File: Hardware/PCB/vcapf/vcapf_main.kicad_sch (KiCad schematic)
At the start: 42 parts, among them Q1 2N3906, Q2 2N3906, U1 LM13700, U2 TL074, U3 TL072

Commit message: Match transistors
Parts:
- Q1, Q2: value 2N3906 -> (none)
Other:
- moved on the sheet: C10, C4, C5, C7, C8, C9, U1B, U1D, U1E, U2E, U3C

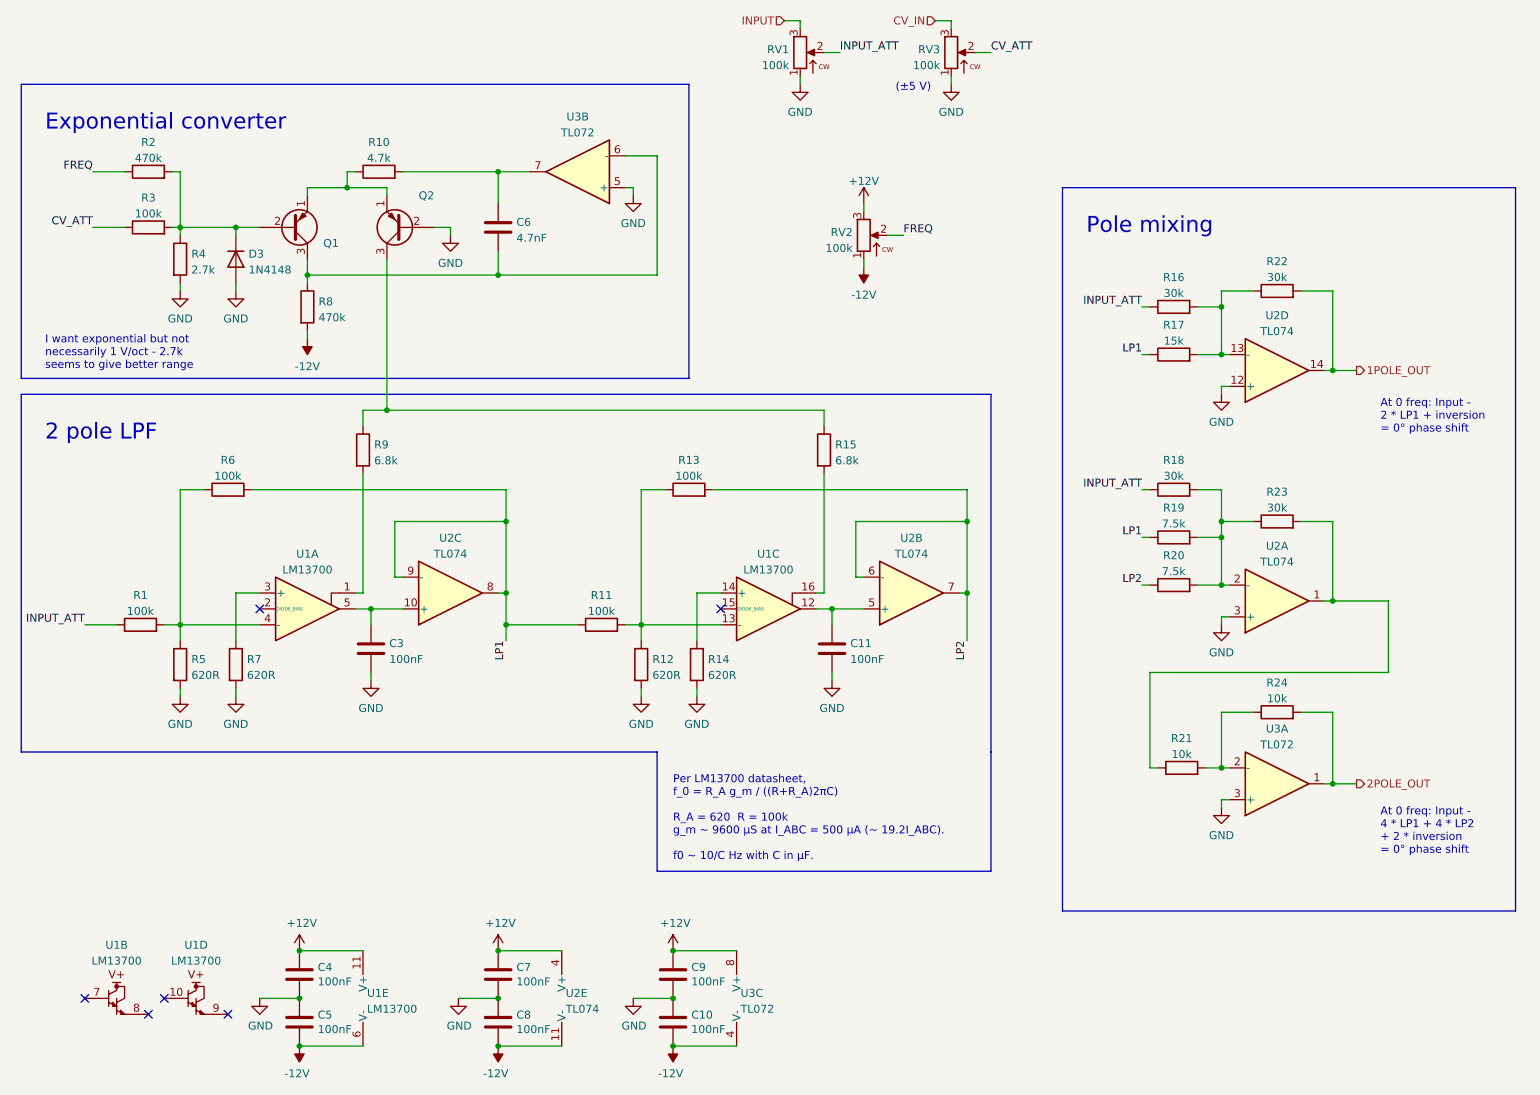
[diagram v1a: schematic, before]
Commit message: Pre fab tweaks, unreverse jacks, Gerbers
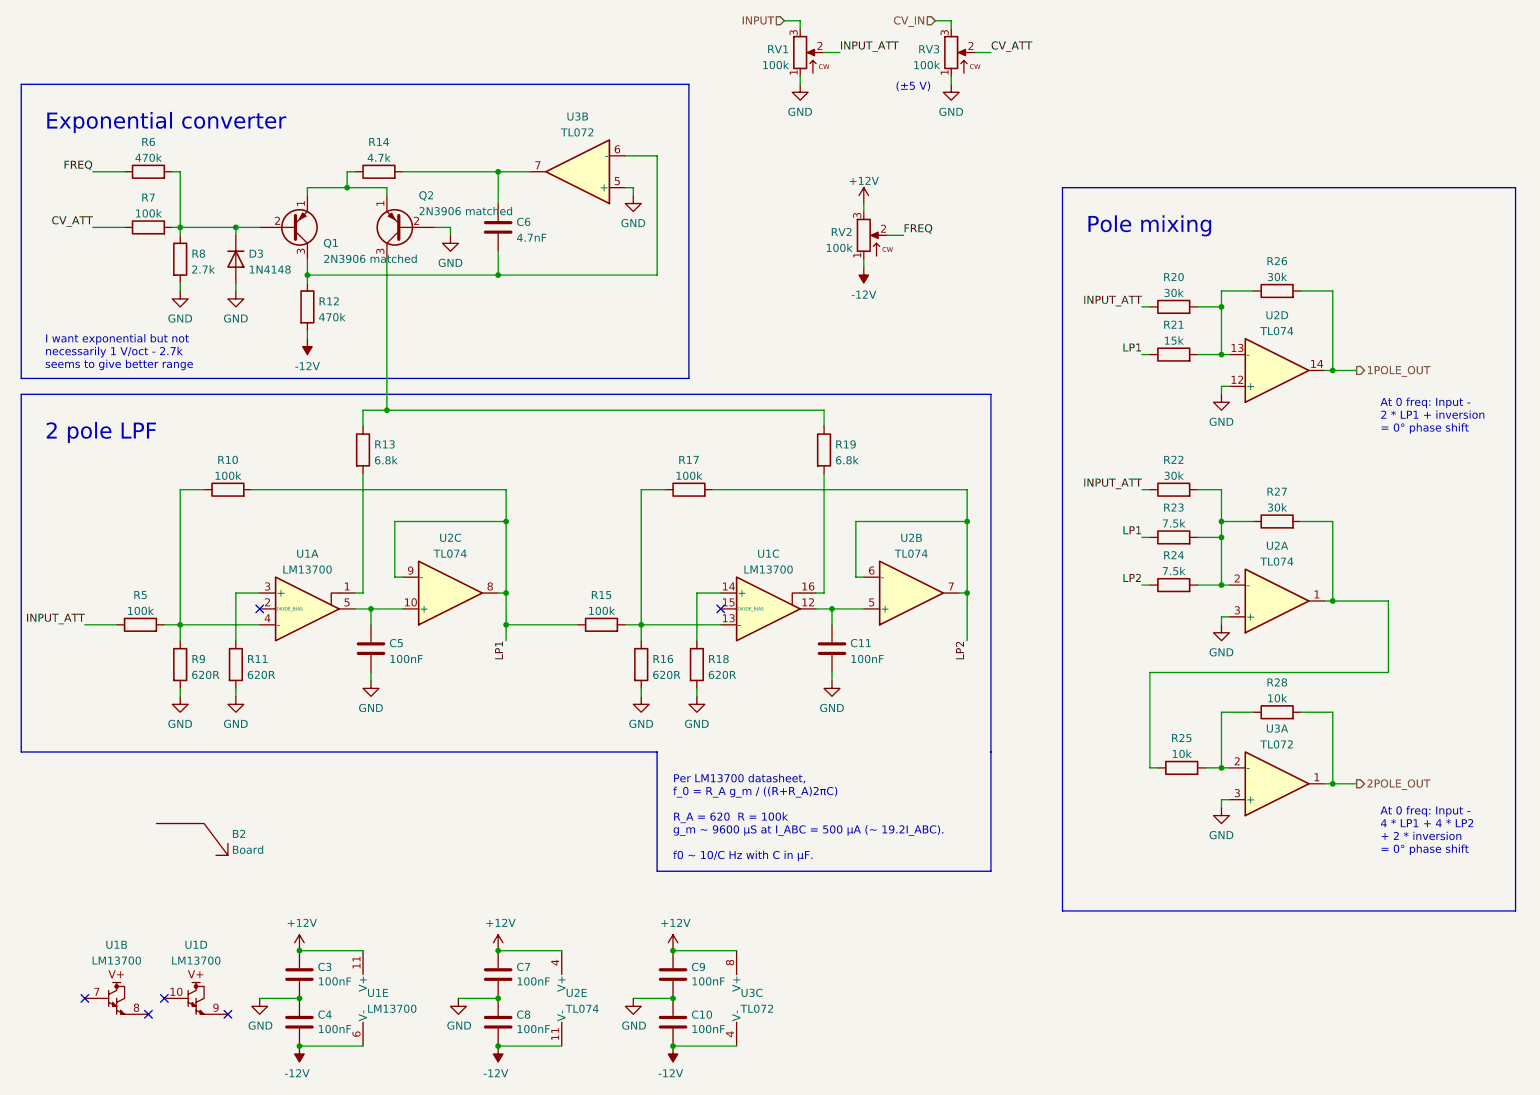
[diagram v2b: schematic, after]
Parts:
- added B2: Board, ao_tht:Board_Marker, symbol ao_symbols:Board
- Q1, Q2: value (none) -> 2N3906 matched
- renumbered C4 to C3, C5 to C4, C3 to C5, R6 to R10, R7 to R11, R8 to R12, R9 to R13, R10 to R14, R11 to R15, R12 to R16, R13 to R17, R14 to R18, R15 to R19, R16 to R20, R17 to R21, R18 to R22, R19 to R23, R20 to R24, R21 to R25, R22 to R26, R23 to R27, R24 to R28, R1 to R5, R2 to R6, R3 to R7, R4 to R8, R5 to R9

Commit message: Post fab updates
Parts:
- C11, C5: SKU (none) -> A-564
- RV1, RV2, RV3: SKU (none) -> A-1628
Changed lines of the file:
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@@
+      (effects (font (size 1.27 1.27)) hide)
+    )
+    (property "Description" "1/4 watt resistor, metal film" (id 5) (at 57.15 125.73 0)
       (effects (font (size 1.27 1.27)) hide)
     )
@@
     )
     (property "SKU" "A-553" (id 5) (at 67.31 175.26 0)
+      (effects (font (size 1.27 1.27)) hide)
+    )
+    (property "Description" "Ceramic capacitor, 2.5 mm pitch" (id 6) (at 67.31 175.26 0)
       (effects (font (size 1.27 1.27)) hide)
     )
@@
       (effects (font (size 1.27 1.27)) hide)
     )
+    (property "Description" "Ceramic capacitor, 2.5 mm pitch" (id 6) (at 127 182.88 0)
+      (effects (font (size 1.27 1.27)) hide)
+    )
     (pin "1")
     (pin "2")
@@
     )
     (property "Vendor" "Tayda" (id 4) (at 48.26 60.96 0)
+      (effects (font (size 1.27 1.27)) hide)
+    )
+    (property "Description" "1/4 watt resistor, metal film" (id 5) (at 48.26 60.96 0)
       (effects (font (size 1.27 1.27)) hide)
     )
@@
       (effects (font (size 1.27 1.27)) hide)
     )
+    (property "Description" "1/4 watt resistor, metal film" (id 5) (at 207.01 105.41 0)
+      (effects (font (size 1.27 1.27)) hide)
+    )
     (pin "1")
     (pin "2")
@@
     )
     (property "Vendor" "Tayda" (id 4) (at 130.81 125.73 0)
+      (effects (font (size 1.27 1.27)) hide)
+    )
+    (property "Description" "1/4 watt resistor, metal film" (id 5) (at 130.81 125.73 0)
       (effects (font (size 1.27 1.27)) hide)
     )
@@
       (effects (font (size 1.27 1.27)) hide)
     )
+    (property "Description" "Ceramic capacitor, 2.5 mm pitch" (id 6) (at 99.06 175.26 0)
+      (effects (font (size 1.27 1.27)) hide)
+    )
     (pin "1")
     (pin "2")
@@
     )
     (property "Vendor" "Tayda" (id 4) (at 68.58 68.58 0)
+      (effects (font (size 1.27 1.27)) hide)
+    )
+    (property "Description" "1/4 watt resistor, metal film" (id 5) (at 68.58 68.58 0)
       (effects (font (size 1.27 1.27)) hide)
     )
@@
       (effects (font (size 1.27 1.27)) hide)
     )
+    (property "Description" "1/4 watt resistor, metal film" (id 5) (at 207.01 68.58 0)
+      (effects (font (size 1.27 1.27)) hide)
+    )
     (pin "1")
     (pin "2")
@@
     )
     (property "Vendor" "Tayda" (id 4) (at 80.01 46.99 0)
+      (effects (font (size 1.27 1.27)) hide)
+    )
+    (property "Description" "1/4 watt resistor, metal film" (id 5) (at 80.01 46.99 0)
       (effects (font (size 1.27 1.27)) hide)
     )
@@
       (effects (font (size 1.27 1.27)) hide)
     )
+    (property "Description" "1/4 watt resistor, metal film" (id 5) (at 208.28 142.24 0)
+      (effects (font (size 1.27 1.27)) hide)
+    )
     (pin "1")
     (pin "2")
@@
     )
     (property "Vendor" "Tayda" (id 4) (at 77.47 91.44 0)
+      (effects (font (size 1.27 1.27)) hide)
+    )
+    (property "Description" "1/4 watt resistor, metal film" (id 5) (at 77.47 91.44 0)
       (effects (font (size 1.27 1.27)) hide)
     )
@@
       (effects (font (size 1.27 1.27)) hide)
     )
+    (property "Description" "1/4 watt resistor, metal film" (id 5) (at 121.92 125.73 0)
+      (effects (font (size 1.27 1.27)) hide)
+    )
     (pin "1")
     (pin "2")
@@
     )
     (property "Vendor" "Tayda" (id 4) (at 41.91 119.38 0)
+      (effects (font (size 1.27 1.27)) hide)
+    )
+    (property "Description" "1/4 watt resistor, metal film" (id 5) (at 41.91 119.38 0)
       (effects (font (size 1.27 1.27)) hide)
     )
@@
       (effects (font (size 1.27 1.27)) hide)
     )
+    (property "Description" "1/4 watt resistor, metal film" (id 5) (at 115.57 119.38 0)
+      (effects (font (size 1.27 1.27)) hide)
+    )
     (pin "1")
     (pin "2")
@@
       (effects (font (size 1.27 1.27)) hide)
     )
+    (property "Description" "Polyester capacitor" (id 5) (at 152.4 123.19 0)
+      (effects (font (size 1.27 1.27)) hide)
+    )
+    (property "SKU" "A-564" (id 6) (at 152.4 123.19 0)
+      (effects (font (size 1.27 1.27)) hide)
+    )
     (pin "1")
     (pin "2")
@@
       (effects (font (size 1.27 1.27)) hide)
     )
+    (property "Description" "1/4 watt resistor, metal film" (id 5) (at 43.18 55.88 0)
+      (effects (font (size 1.27 1.27)) hide)
+    )
     (pin "1")
     (pin "2")
@@
     )
     (property "Vendor" "Tayda" (id 4) (at 99.06 55.88 0)
+      (effects (font (size 1.27 1.27)) hide)
+    )
+    (property "Description" "Ceramic capacitor, 2.5 mm pitch" (id 5) (at 99.06 55.88 0)
       (effects (font (size 1.27 1.27)) hide)
     )
@@
       (effects (font (size 1.27 1.27)) hide)
     )
+    (property "Description" "Ceramic capacitor, 2.5 mm pitch" (id 6) (at 127 175.26 0)
+      (effects (font (size 1.27 1.27)) hide)
+    )
     (pin "1")
     (pin "2")
@@
     )
     (property "Vendor" "Tayda" (id 4) (at 151.13 91.44 0)
+      (effects (font (size 1.27 1.27)) hide)
+    )
+    (property "Description" "1/4 watt resistor, metal film" (id 5) (at 151.13 91.44 0)
       (effects (font (size 1.27 1.27)) hide)
     )
@@
     )
     (property "Vendor" "Tayda" (id 4) (at 171.45 27.94 0)
+      (effects (font (size 1.27 1.27)) hide)
+    )
+    (property "Description" "Linear potentiometer, 16 mm, PCB mount, vertical" (id 5) (at 171.45 27.94 0)
+      (effects (font (size 1.27 1.27)) hide)
+    )
+    (property "SKU" "A-1628" (id 6) (at 171.45 27.94 0)
       (effects (font (size 1.27 1.27)) hide)
     )
@@
     )
     (property "SKU" "A-553" (id 5) (at 99.06 182.88 0)
+      (effects (font (size 1.27 1.27)) hide)
+    )
+    (property "Description" "Ceramic capacitor, 2.5 mm pitch" (id 6) (at 99.06 182.88 0)
       (effects (font (size 1.27 1.27)) hide)
     )
@@
       (effects (font (size 1.27 1.27)) hide)
     )
+    (property "Description" "1/4 watt resistor, metal film" (id 5) (at 207.01 76.2 0)
+      (effects (font (size 1.27 1.27)) hide)
+    )
     (pin "1")
     (pin "2")
@@
       (effects (font (size 1.27 1.27)) hide)
     )
+    (property "Description" "1/4 watt resistor, metal film" (id 5) (at 223.52 66.04 0)
+      (effects (font (size 1.27 1.27)) hide)
+    )
     (pin "1")
     (pin "2")
@@
     )
     (property "Vendor" "Tayda" (id 4) (at 223.52 133.35 0)
+      (effects (font (size 1.27 1.27)) hide)
+    )
+    (property "Description" "1/4 watt resistor, metal film" (id 5) (at 223.52 133.35 0)
       (effects (font (size 1.27 1.27)) hide)
     )
@@
       (effects (font (size 1.27 1.27)) hide)
     )
+    (property "Description" "Linear potentiometer, 16 mm, PCB mount, vertical" (id 5) (at 157.48 57.15 0)
+      (effects (font (size 1.27 1.27)) hide)
+    )
+    (property "SKU" "A-1628" (id 6) (at 157.48 57.15 0)
+      (effects (font (size 1.27 1.27)) hide)
+    )
     (pin "1")
     (pin "2")
@@
       (effects (font (size 1.27 1.27)) hide)
     )
+    (property "Description" "1/4 watt resistor, metal film" (id 5) (at 55.88 97.79 0)
+      (effects (font (size 1.27 1.27)) hide)
+    )
     (pin "1")
     (pin "2")
@@
     )
     (property "Vendor" "Tayda" (id 4) (at 207.01 113.03 0)
+      (effects (font (size 1.27 1.27)) hide)
+    )
+    (property "Description" "1/4 watt resistor, metal film" (id 5) (at 207.01 113.03 0)
       (effects (font (size 1.27 1.27)) hide)
     )
@@
       (effects (font (size 1.27 1.27)) hide)
     )
+    (property "Description" "Ceramic capacitor, 2.5 mm pitch" (id 6) (at 67.31 182.88 0)
+      (effects (font (size 1.27 1.27)) hide)
+    )
     (pin "1")
     (pin "2")
@@
       (effects (font (size 1.27 1.27)) hide)
     )
+    (property "Description" "1/4 watt resistor, metal film" (id 5) (at 223.52 102.87 0)
+      (effects (font (size 1.27 1.27)) hide)
+    )
     (pin "1")
     (pin "2")
@@
     )
     (property "Vendor" "Tayda" (id 4) (at 48.26 125.73 0)
+      (effects (font (size 1.27 1.27)) hide)
+    )
+    (property "Description" "1/4 watt resistor, metal film" (id 5) (at 48.26 125.73 0)
       (effects (font (size 1.27 1.27)) hide)
     )
@@
     )
     (property "Vendor" "Tayda" (id 4) (at 129.54 97.79 0)
+      (effects (font (size 1.27 1.27)) hide)
+    )
+    (property "Description" "1/4 watt resistor, metal film" (id 5) (at 129.54 97.79 0)
       (effects (font (size 1.27 1.27)) hide)
     )
@@
       (effects (font (size 1.27 1.27)) hide)
     )
+    (property "Description" "1/4 watt resistor, metal film" (id 5) (at 43.18 46.99 0)
+      (effects (font (size 1.27 1.27)) hide)
+    )
     (pin "1")
     (pin "2")
@@
       (effects (font (size 1.27 1.27)) hide)
     )
+    (property "Description" "1/4 watt resistor, metal film" (id 5) (at 207.01 97.79 0)
+      (effects (font (size 1.27 1.27)) hide)
+    )
     (pin "1")
     (pin "2")
@@
     )
     (property "Vendor" "Tayda" (id 4) (at 78.74 123.19 0)
+      (effects (font (size 1.27 1.27)) hide)
+    )
+    (property "Description" "Polyester capacitor" (id 5) (at 78.74 123.19 0)
+      (effects (font (size 1.27 1.27)) hide)
+    )
+    (property "SKU" "A-564" (id 6) (at 78.74 123.19 0)
       (effects (font (size 1.27 1.27)) hide)
     )
@@
       (effects (font (size 1.27 1.27)) hide)
     )
+    (property "Description" "Linear potentiometer, 16 mm, PCB mount, vertical" (id 5) (at 147.32 27.94 0)
+      (effects (font (size 1.27 1.27)) hide)
+    )
+    (property "SKU" "A-1628" (id 6) (at 147.32 27.94 0)
+      (effects (font (size 1.27 1.27)) hide)
+    )
